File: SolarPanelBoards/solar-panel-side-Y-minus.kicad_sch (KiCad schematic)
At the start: 52 parts, among them J1 Conn_01x06, Q1 MBT2222ADW1T1, Q2 MBT2222ADW1T1, Q3 BSS138DWQ-7, Q4 BSS138DWQ-7, U1 OPT3001DNPT, U2 DRV8830DGQR

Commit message: Y minus updates
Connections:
- net +3V3: no longer U1.2 (ADDR)
- net GND: now also U1.2 (ADDR)
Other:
- note added: "x47"
- note removed: "x46"
- company: SSI Satellite Team -> (none)
- title: SolarPanel+-Y -> (none)
- moved on the sheet: C1

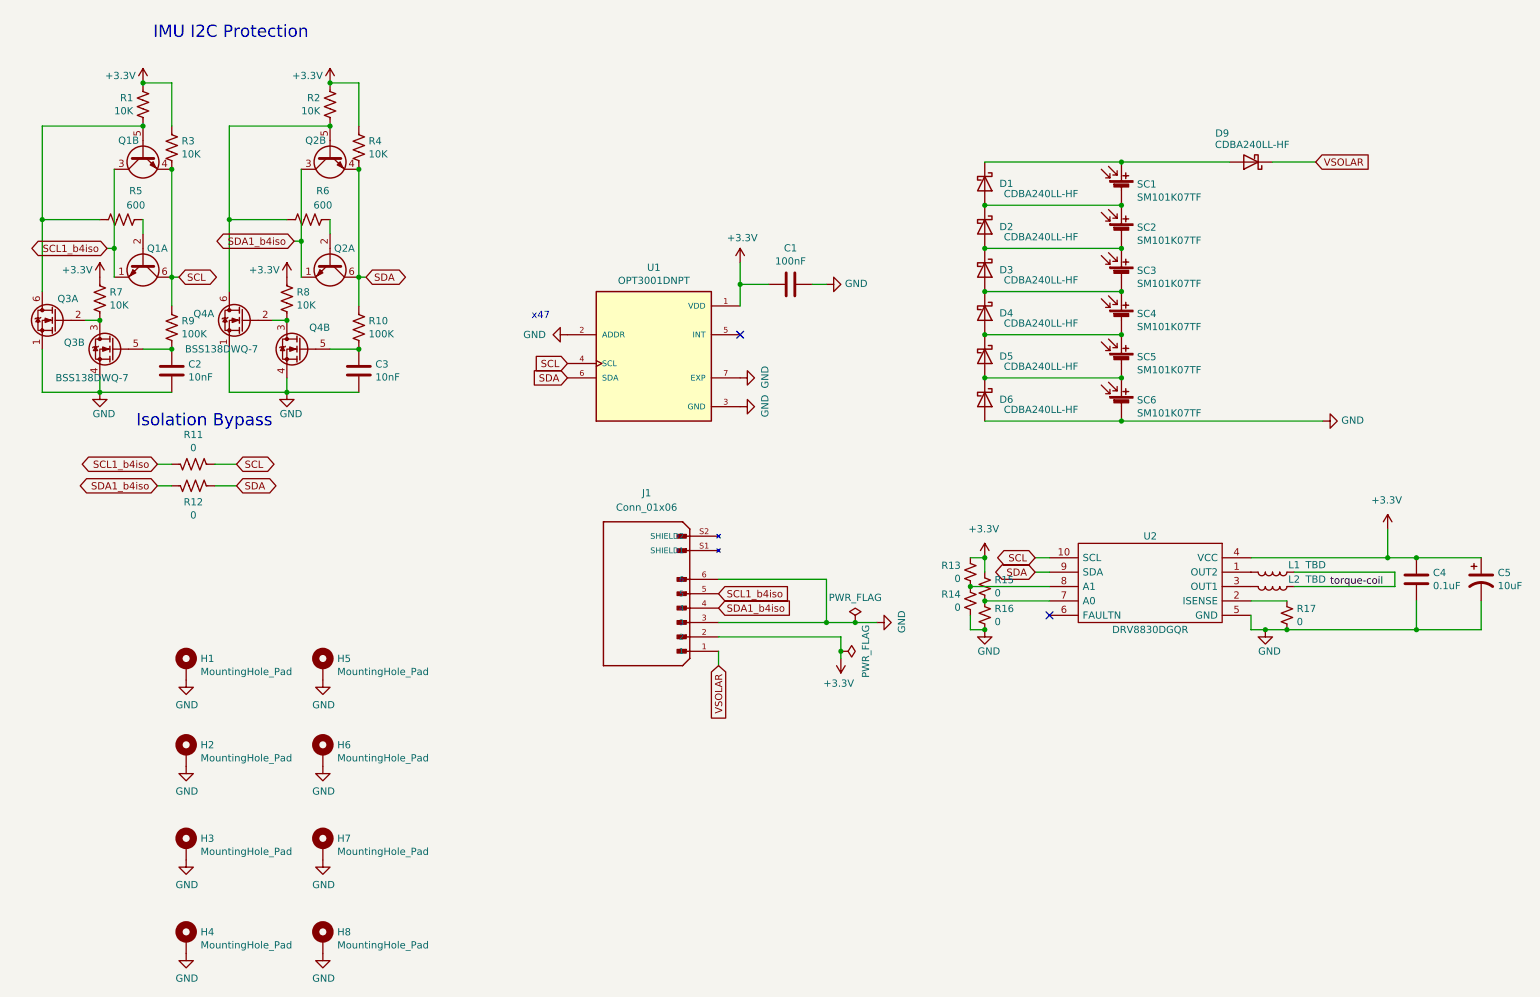
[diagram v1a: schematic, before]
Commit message: footprint for U2
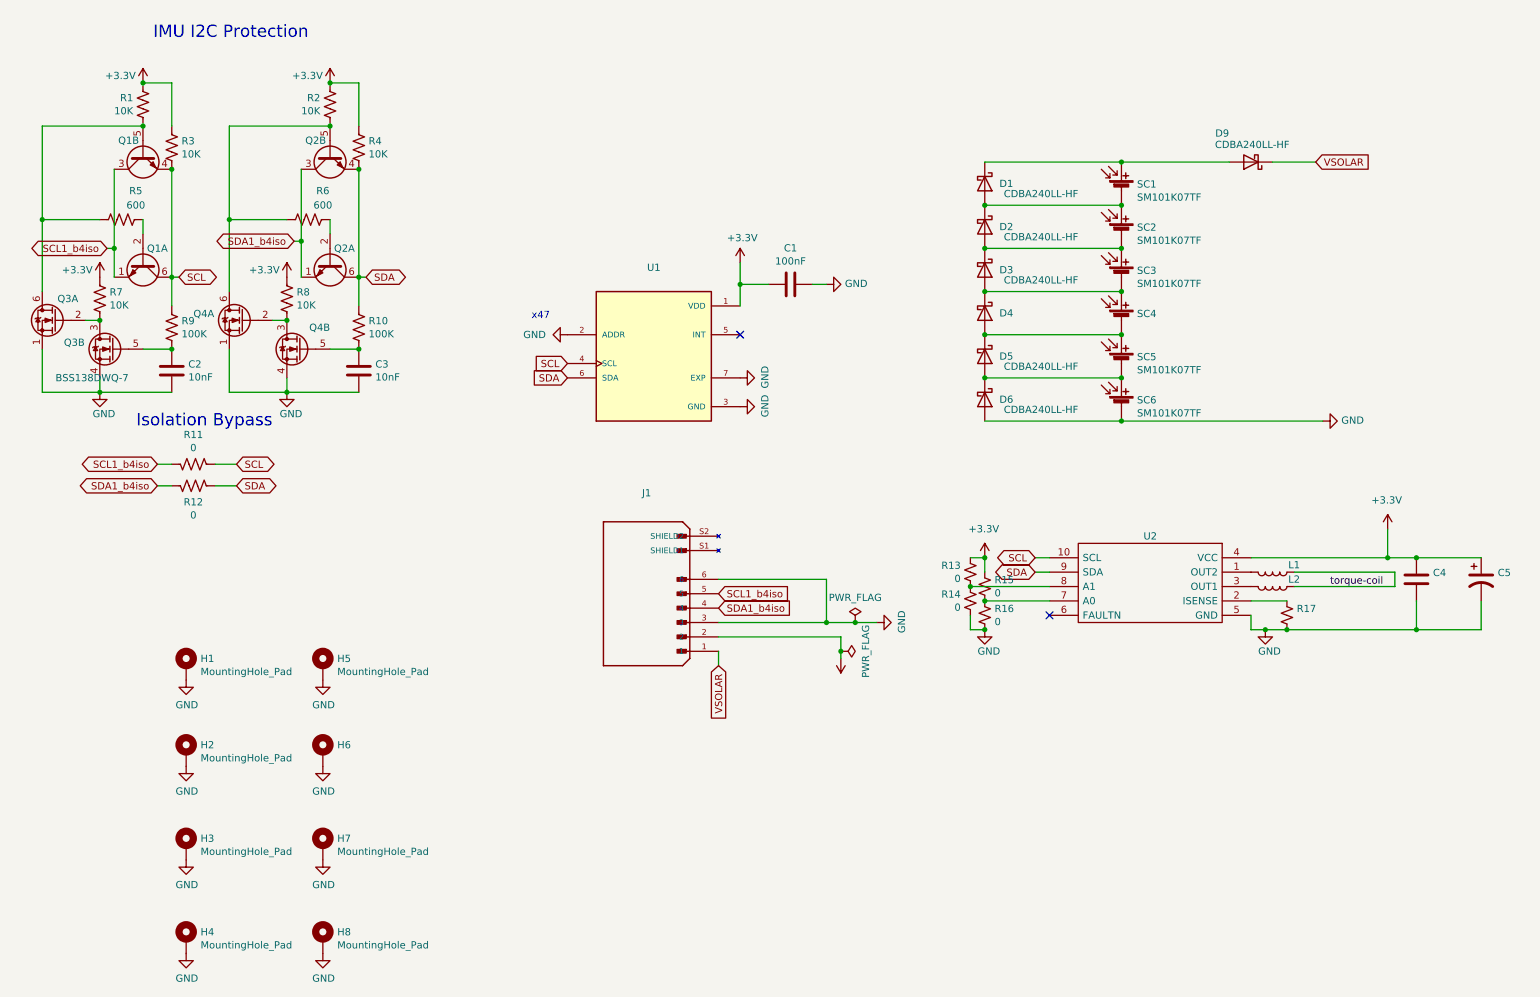
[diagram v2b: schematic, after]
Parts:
- C4: value 0.1uF -> (none); footprint Capacitor_SMD:C_0402_1005Metric -> (none)
- C5: value 10uF -> (none); footprint Capacitor_SMD:C_0805_2012Metric -> (none)
- D4: value CDBA240LL-HF -> (none); footprint sapling:DO-214AC -> (none)
- H6: value MountingHole_Pad -> (none); footprint MountingHole:MountingHole_2.2mm_M2_DIN965_Pad_TopBottom -> (none)
- J1: value Conn_01x06 -> (none); footprint sapling:MOLEX_2053380006 -> (none)
- L1, L2: value TBD -> (none); footprint Inductor_SMD:L_0603_1608Metric -> (none)
- Q1: value MBT2222ADW1T1 -> (none); footprint Package_TO_SOT_SMD:SOT-363_SC-70-6 -> (none)
- Q4: value BSS138DWQ-7 -> (none); footprint custom-footprints:BSS138DWQ-7 -> (none)
- R17: value 0 -> (none); footprint Resistor_SMD:R_0402_1005Metric -> (none)
- SC4: value SM101K07TF -> (none); footprint sapling:SM101K07TF -> (none)
- U1: value OPT3001DNPT -> (none); footprint sapling:OPT3001 -> (none)
- U2: value DRV8830DGQR -> (none)
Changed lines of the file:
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@@
   (global_label "VSOLAR" (shape input) (at 138.43 129.54 270) (fields_autoplaced)
     (effects (font (size 1.27 1.27)) (justify right))
-    (property "Intersheet References" "${INTERSHEET_REFS}" (id 0) (at -29.21 -8.89 0)
-      (effects (font (size 1.27 1.27)) hide)
+    (property "Intersheet References" "${INTERSHEET_REFS}" (id 0) (at 138.3506 138.8794 90)
+      (effects (font (size 1.27 1.27)) (justify right) hide)
     )
   )
@@
     (in_bom yes) (on_board yes)
     (property "Reference" "D4" (id 0) (at 189.23 67.31 90))
-    (property "Value" "CDBA240LL-HF" (id 1) (at 201.93 69.85 90)
+    (property "Value" "" (id 1) (at 201.93 69.85 90)
       (effects (font (size 1.27 1.27)) (justify right bottom))
     )
-    (property "Footprint" "sapling:DO-214AC" (id 2) (at 185.42 67.31 0)
+    (property "Footprint" "" (id 2) (at 185.42 67.31 0)
       (effects (font (size 1.27 1.27)) hide)
     )
@@
       (effects (font (size 1.27 1.27)) (justify left))
     )
-    (property "Value" "MountingHole_Pad" (id 1) (at 71.12 145.8468 0)
-      (effects (font (size 1.27 1.27)) (justify left))
-    )
-    (property "Footprint" "MountingHole:MountingHole_2.2mm_M2_DIN965_Pad_TopBottom" (id 2) (at 68.58 144.78 0)
+    (property "Value" "" (id 1) (at 71.12 145.8468 0)
+      (effects (font (size 1.27 1.27)) (justify left))
+    )
+    (property "Footprint" "" (id 2) (at 68.58 144.78 0)
       (effects (font (size 1.27 1.27)) hide)
     )
@@
       (effects (font (size 1.27 1.27)) (justify left))
     )
-    (property "Value" "SM101K07TF" (id 1) (at 212.2932 69.723 0)
-      (effects (font (size 1.27 1.27)) (justify left))
-    )
-    (property "Footprint" "sapling:SM101K07TF" (id 2) (at 209.55 67.056 90)
+    (property "Value" "" (id 1) (at 212.2932 69.723 0)
+      (effects (font (size 1.27 1.27)) (justify left))
+    )
+    (property "Footprint" "" (id 2) (at 209.55 67.056 90)
       (effects (font (size 1.27 1.27)) hide)
     )
@@
       (effects (font (size 1.27 1.27)) hide)
     )
-    (property "Value" "+3.3V" (id 1) (at 159.639 132.6642 0))
+    (property "Value" "" (id 1) (at 159.639 132.6642 0))
     (property "Footprint" "" (id 2) (at 160.02 128.27 0)
       (effects (font (size 1.27 1.27)) hide)
@@
     (in_bom yes) (on_board yes)
     (property "Reference" "J1" (id 0) (at 125.73 99.06 0))
-    (property "Value" "Conn_01x06" (id 1) (at 125.73 101.6 0))
-    (property "Footprint" "sapling:MOLEX_2053380006" (id 2) (at 125.73 116.84 0)
+    (property "Value" "" (id 1) (at 125.73 101.6 0))
+    (property "Footprint" "" (id 2) (at 125.73 116.84 0)
       (effects (font (size 1.27 1.27)) hide)
     )
@@
       (effects (font (size 1.27 1.27)) (justify left))
     )
-    (property "Value" "BSS138DWQ-7" (id 1) (at 59.563 74.803 0)
-      (effects (font (size 1.27 1.27)) (justify left) hide)
-    )
-    (property "Footprint" "custom-footprints:BSS138DWQ-7" (id 2) (at 59.69 69.85 0)
+    (property "Value" "" (id 1) (at 59.563 74.803 0)
+      (effects (font (size 1.27 1.27)) (justify left) hide)
+    )
+    (property "Footprint" "" (id 2) (at 59.69 69.85 0)
       (effects (font (size 1.27 1.27)) (justify left) hide)
     )
@@
     (in_bom yes) (on_board yes)
     (property "Reference" "Q1" (id 0) (at 34.29 36.83 90))
-    (property "Value" "MBT2222ADW1T1" (id 1) (at 36.83 20.32 90)
-      (effects (font (size 1.27 1.27)) hide)
-    )
-    (property "Footprint" "Package_TO_SOT_SMD:SOT-363_SC-70-6" (id 2) (at 34.29 44.45 0)
+    (property "Value" "" (id 1) (at 36.83 20.32 90)
+      (effects (font (size 1.27 1.27)) hide)
+    )
+    (property "Footprint" "" (id 2) (at 34.29 44.45 0)
       (effects (font (size 1.27 1.27)) hide)
     )
@@
     (in_bom yes) (on_board yes)
     (property "Reference" "U2" (id 0) (at 214.63 106.68 0))
-    (property "Value" "DRV8830DGQR" (id 1) (at 214.63 123.19 0))
+    (property "Value" "" (id 1) (at 214.63 123.19 0))
     (property "Footprint" "" (id 2) (at 182.88 113.03 0)
       (effects (font (size 1.27 1.27)) (justify left) hide)
@@
       (effects (font (size 1.27 1.27)) (justify left))
     )
-    (property "Value" "0.1uF" (id 1) (at 264.541 115.443 0)
-      (effects (font (size 1.27 1.27)) (justify left))
-    )
-    (property "Footprint" "Capacitor_SMD:C_0402_1005Metric" (id 2) (at 262.5852 118.11 0)
+    (property "Value" "" (id 1) (at 264.541 115.443 0)
+      (effects (font (size 1.27 1.27)) (justify left))
+    )
+    (property "Footprint" "" (id 2) (at 262.5852 118.11 0)
       (effects (font (size 1.27 1.27)) hide)
     )
@@
       (effects (font (size 1.27 1.27)) (justify left))
     )
-    (property "Value" "BSS138DWQ-7" (id 1) (at 57.15 73.66 0)
-      (effects (font (size 1.27 1.27)) (justify left))
-    )
-    (property "Footprint" "custom-footprints:BSS138DWQ-7" (id 2) (at 49.53 64.77 0)
+    (property "Value" "" (id 1) (at 57.15 73.66 0)
+      (effects (font (size 1.27 1.27)) (justify left))
+    )
+    (property "Footprint" "" (id 2) (at 49.53 64.77 0)
       (effects (font (size 1.27 1.27)) (justify left) hide)
     )
@@
       (effects (font (size 1.27 1.27)) (justify left))
     )
-    (property "Value" "10uF" (id 1) (at 275.971 115.443 0)
-      (effects (font (size 1.27 1.27)) (justify left))
-    )
-    (property "Footprint" "Capacitor_SMD:C_0805_2012Metric" (id 2) (at 273.05 114.3 0)
+    (property "Value" "" (id 1) (at 275.971 115.443 0)
+      (effects (font (size 1.27 1.27)) (justify left))
+    )
+    (property "Footprint" "" (id 2) (at 273.05 114.3 0)
       (effects (font (size 1.27 1.27)) hide)
     )
@@
     (in_bom yes) (on_board yes)
     (property "Reference" "L1" (id 0) (at 240.03 111.76 90))
-    (property "Value" "TBD" (id 1) (at 243.84 111.76 90))
-    (property "Footprint" "Inductor_SMD:L_0603_1608Metric" (id 2) (at 236.22 113.03 0)
+    (property "Value" "" (id 1) (at 243.84 111.76 90))
+    (property "Footprint" "" (id 2) (at 236.22 113.03 0)
       (effects (font (size 1.27 1.27)) hide)
     )
@@
     (in_bom yes) (on_board yes)
     (property "Reference" "U1" (id 0) (at 127 59.2582 0))
-    (property "Value" "OPT3001DNPT" (id 1) (at 127 61.5696 0))
-    (property "Footprint" "sapling:OPT3001" (id 2) (at 121.92 60.96 0)
+    (property "Value" "" (id 1) (at 127 61.5696 0))
+    (property "Footprint" "" (id 2) (at 121.92 60.96 0)
       (effects (font (size 1.27 1.27)) (justify left bottom) hide)
     )
@@
     (in_bom yes) (on_board yes)
     (property "Reference" "L2" (id 0) (at 240.03 114.3 90))
-    (property "Value" "TBD" (id 1) (at 243.84 114.3 90))
-    (property "Footprint" "Inductor_SMD:L_0603_1608Metric" (id 2) (at 236.22 115.57 0)
+    (property "Value" "" (id 1) (at 243.84 114.3 90))
+    (property "Footprint" "" (id 2) (at 236.22 115.57 0)
       (effects (font (size 1.27 1.27)) hide)
     )
@@
     (in_bom yes) (on_board yes)
     (property "Reference" "Q1" (id 0) (at 39.37 55.88 90))
-    (property "Value" "MBT2222ADW1T1" (id 1) (at 36.83 67.31 90)
-      (effects (font (size 1.27 1.27)) hide)
-    )
-    (property "Footprint" "Package_TO_SOT_SMD:SOT-363_SC-70-6" (id 2) (at 39.37 63.5 0)
+    (property "Value" "" (id 1) (at 36.83 67.31 90)
+      (effects (font (size 1.27 1.27)) hide)
+    )
+    (property "Footprint" "" (id 2) (at 39.37 63.5 0)
       (effects (font (size 1.27 1.27)) hide)
     )
@@
       (effects (font (size 1.27 1.27)) (justify right))
     )
-    (property "Value" "0" (id 1) (at 240.4872 121.793 0)
-      (effects (font (size 1.27 1.27)) (justify right))
-    )
-    (property "Footprint" "Resistor_SMD:R_0402_1005Metric" (id 2) (at 238.76 120.65 0)
+    (property "Value" "" (id 1) (at 240.4872 121.793 0)
+      (effects (font (size 1.27 1.27)) (justify right))
+    )
+    (property "Footprint" "" (id 2) (at 238.76 120.65 0)
       (effects (font (size 1.27 1.27)) hide)
     )
@@
     )
     (path "/2f4b045d-3607-4126-abca-b110031c367b"
-      (reference "U2") (unit 1) (value "DRV8830DGQR") (footprint "")
-    )
-  )
+      (reference "U2") (unit 1) (value "DRV8830DGQR") (footprint "sapling:DRV8830DGQ")
+    )
+  )
